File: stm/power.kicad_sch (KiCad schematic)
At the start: 12 parts, among them J3 USB_C_Receptacle_USB2.0_16P, U4 LM1117MP-ADJ

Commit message: usbc power and uart
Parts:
- added C32: .01u, Capacitor_SMD:C_0603_1608Metric, symbol Device:C
- added C44: .1u, Capacitor_SMD:C_0603_1608Metric, symbol Device:C
- added C45: 4.7u, Capacitor_SMD:CP_Elec_6.3x7.7, symbol Device:C_Polarized
- added D7, D8: ESD9B5.0ST5G, Diode_SMD:D_SOD-923, symbol Diode:ESD9B5.0ST5G
- added F1: 500mA, Fuse:Fuse_1812_4532Metric, symbol Device:Polyfuse
- added FB1: 120, Inductor_SMD:L_0603_1608Metric, symbol Device:FerriteBead
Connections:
- net +5V: now also F1.2
- net GND: now also R24.1, R25.1, C32.2, C44.2, C45.2, D7.1 (A1), D8.1 (A1); no longer R24.2, R25.2
- net PWR_IN: now reaches J3.A4 (VBUS), J3.A9 (VBUS), J3.B4 (VBUS), J3.B9 (VBUS)
- net PWR_IN: now also C32.1, FB1.1
- net at J3.A5 (CC1): now also R25.2; no longer R25.1
- net USBC_D.P: now reaches J3.A6 (D+)
- net USBC_D.P: now also J3.B6 (D+), D7.2 (A2)
- net USBC_D.N: now reaches J3.A7 (D-)
- net USBC_D.N: now also J3.B7 (D-), D8.2 (A2)
- net at J3.B5 (CC2): now also R24.2; no longer R24.1
- new net: C44.1, C45.1, F1.1, FB1.2
- no-connect marks 1 -> 3
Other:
- moved on the sheet: C30, C31, D5, D6, J3, R20, R21, R22, R23, R24, R25, U4

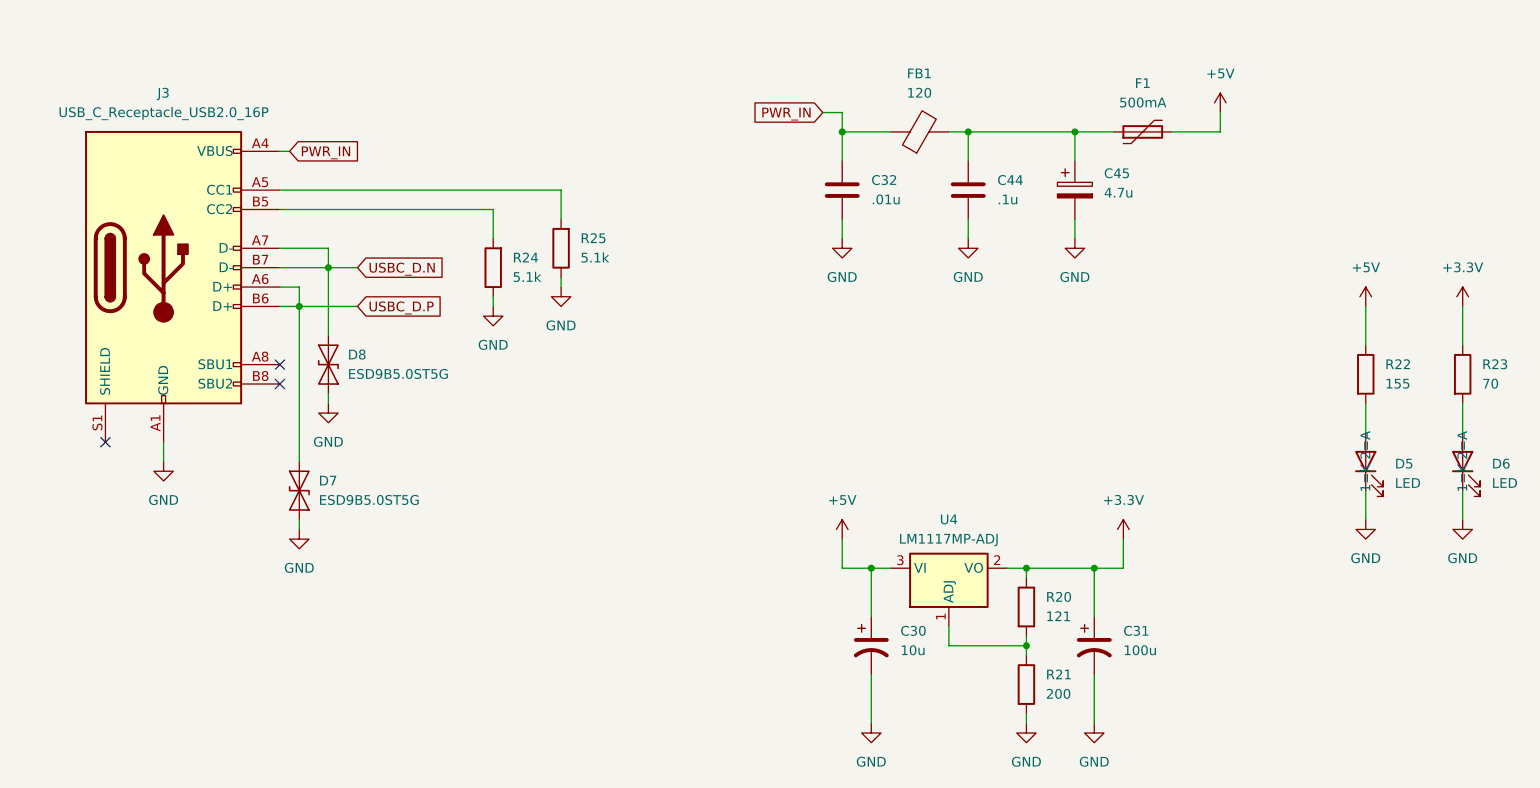
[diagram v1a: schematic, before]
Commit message: usb to uart fix
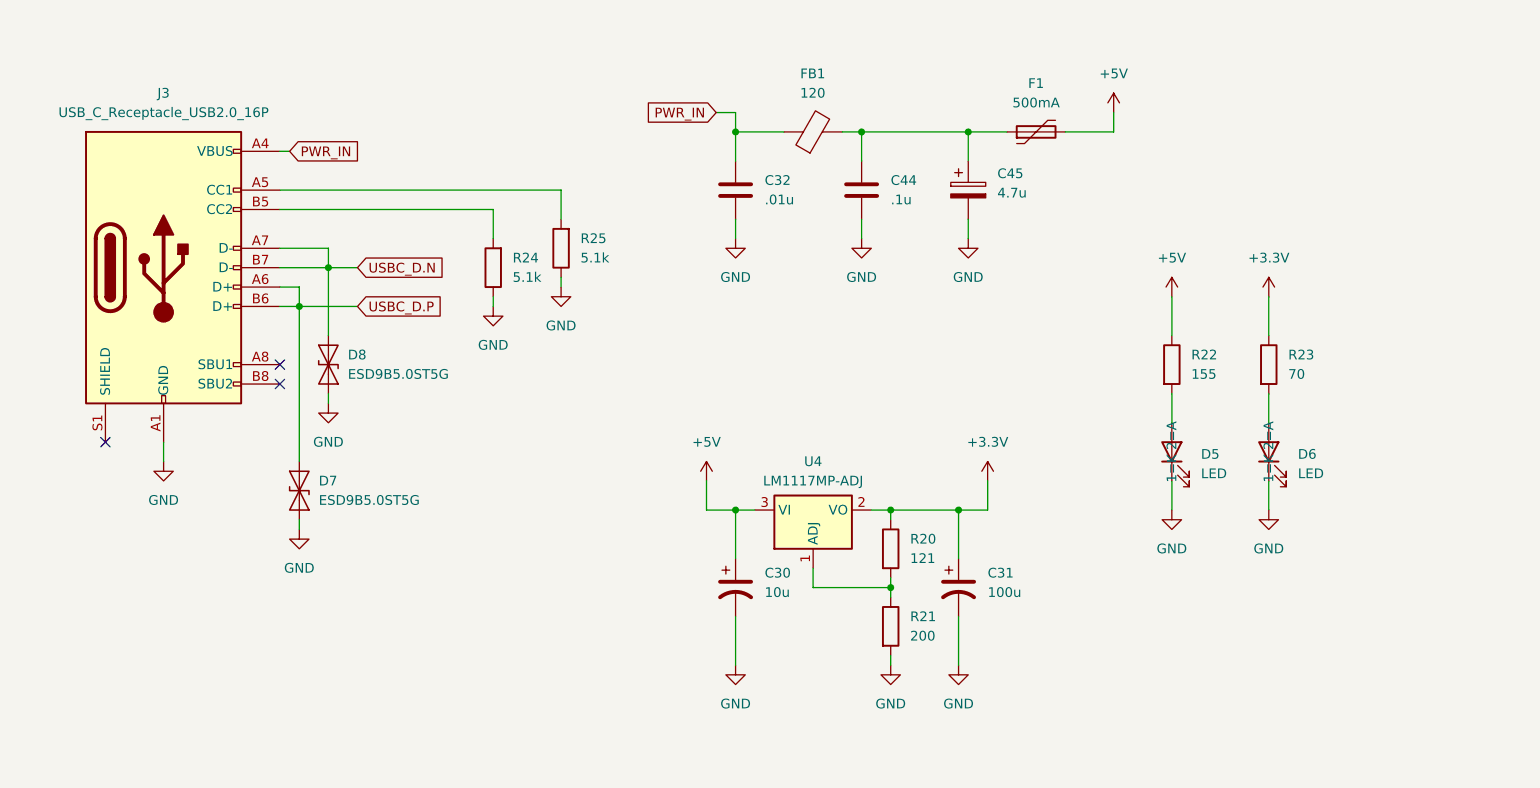
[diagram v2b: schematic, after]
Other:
- moved on the sheet: C30, C31, C32, C44, C45, D5, D6, F1, FB1, R20, R21, R22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

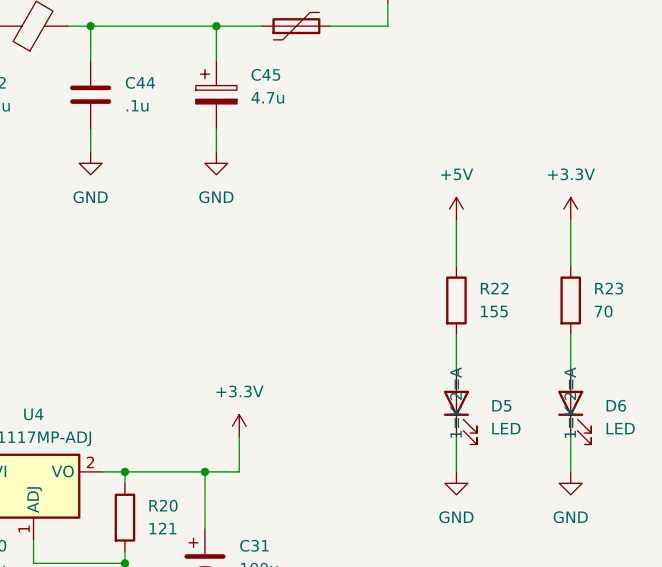
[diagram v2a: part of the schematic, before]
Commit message: changed 3.3V to 3V3
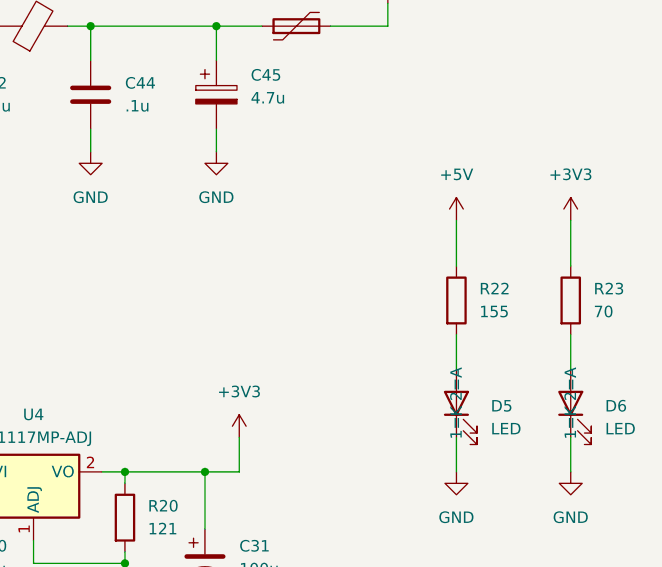
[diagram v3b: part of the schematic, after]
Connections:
- net +3.3V renamed +3V3
